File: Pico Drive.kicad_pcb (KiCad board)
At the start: 2 copper layers, 79.2 x 56.2 mm, 27 parts, among them J1 Conn_01x06_Male, J2 Conn_01x05, J3 Conn_01x03_Male, J4 Conn_01x06, J6 I2C, SW1 Reset, U1 Pico, U2 74AXP1T45GWH, U3 74AHCT1G125DBVTG4

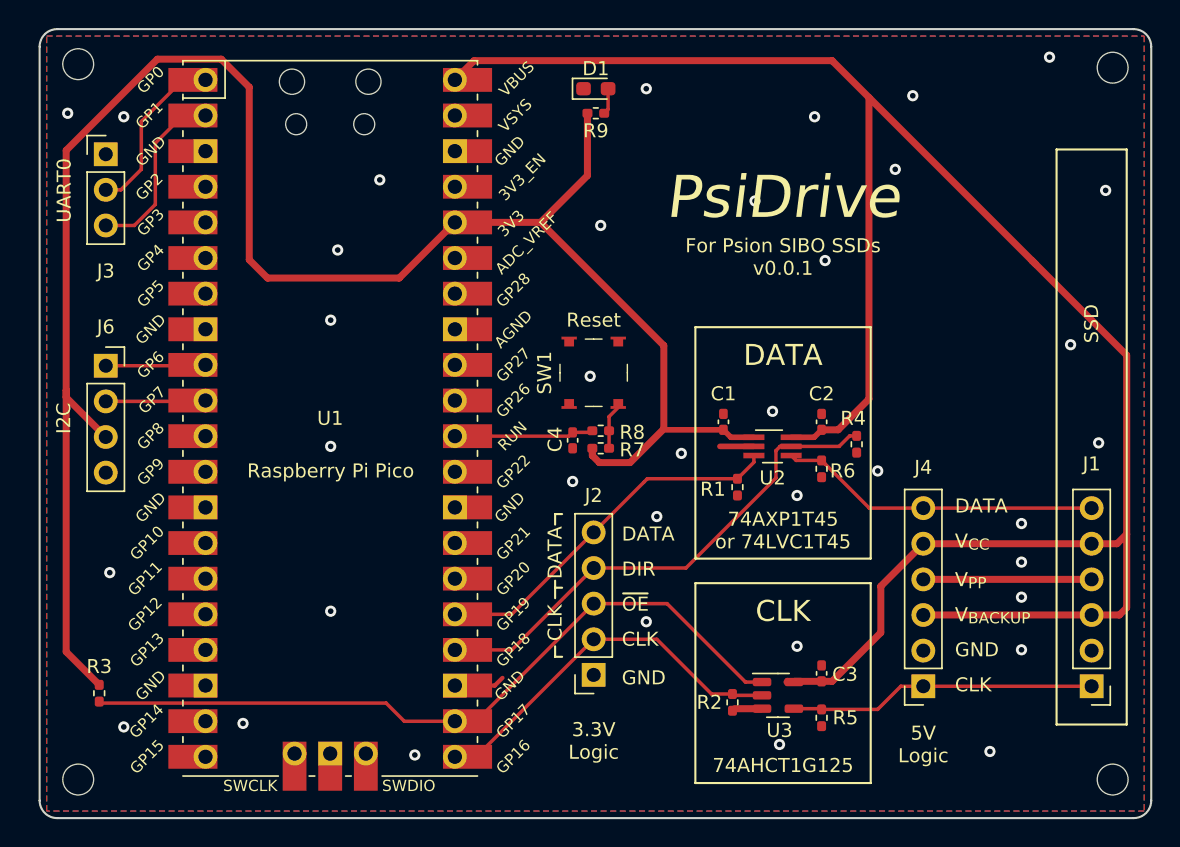
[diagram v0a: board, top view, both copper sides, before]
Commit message: Changed all 0402 components to 0805
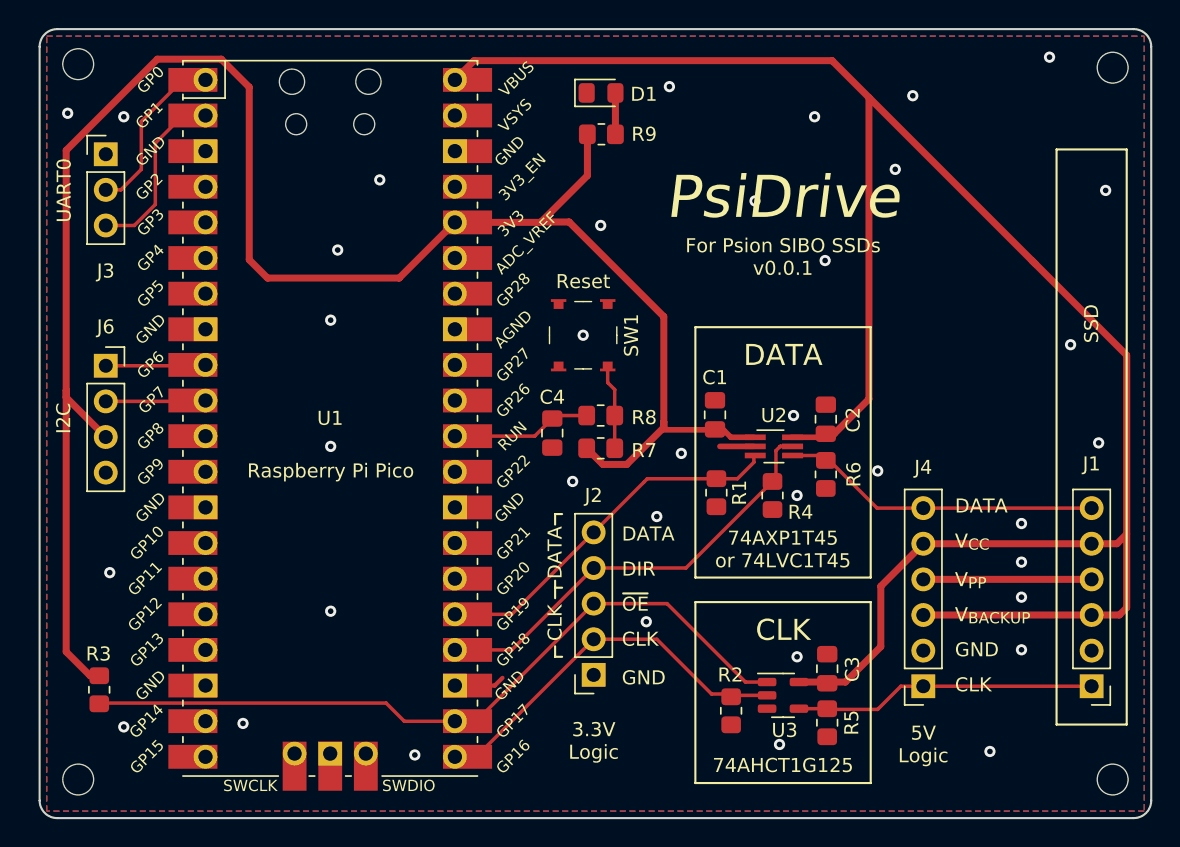
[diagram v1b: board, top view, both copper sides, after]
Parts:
- C1, C2, C3, C4: footprint Capacitor_SMD:C_0402_1005Metric_Pad0.74x0.62mm_HandSolder -> Capacitor_SMD:C_0805_2012Metric_Pad1.18x1.45mm_HandSolder
- D1: footprint LED_SMD:LED_0603_1608Metric_Pad1.05x0.95mm_HandSolder -> LED_SMD:LED_0805_2012Metric_Pad1.15x1.40mm_HandSolder
- R1, R2, R3, R4, R5, R6, R7, R8, R9: footprint Resistor_SMD:R_0402_1005Metric_Pad0.72x0.64mm_HandSolder -> Resistor_SMD:R_0805_2012Metric_Pad1.20x1.40mm_HandSolder
- moved R4 7.02 mm to (68.0, 54.5)
- moved SW1 2.78 mm to (54.5, 43.1)
- moved R1 1.55 mm to (64.0, 54.3)
- moved R9 1.55 mm to (55.8, 28.8)
- moved C4 1.54 mm to (52.3, 50.0)
- moved R8 1.09 mm to (55.8, 48.8)
- moved C1 0.78 mm to (63.9, 48.8)
- moved R2 0.61 mm to (65.0, 69.8)
- moved R5 0.53 mm to (71.9, 70.7)
- moved C3 0.52 mm to (71.9, 66.8)
- moved R6 0.50 mm to (71.8, 53.0)
- moved D1 0.48 mm to (55.8, 25.8)
- moved U3 0.36 mm to (68.8, 68.8)
- moved C2 0.35 mm to (71.8, 49.1)
- moved R3 0.25 mm to (20.0, 68.3)
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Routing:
- net /DATA_DIR: track 36.9 -> 31.9 mm
- net Net-(R7-Pad2): track 3.18 -> 5.79 mm
- net GND: track 8.21 -> 6.04 mm
- net Net-(D1-A): track 1.86 -> 2.95 mm

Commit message: Swapped LED and reset switch, made more space
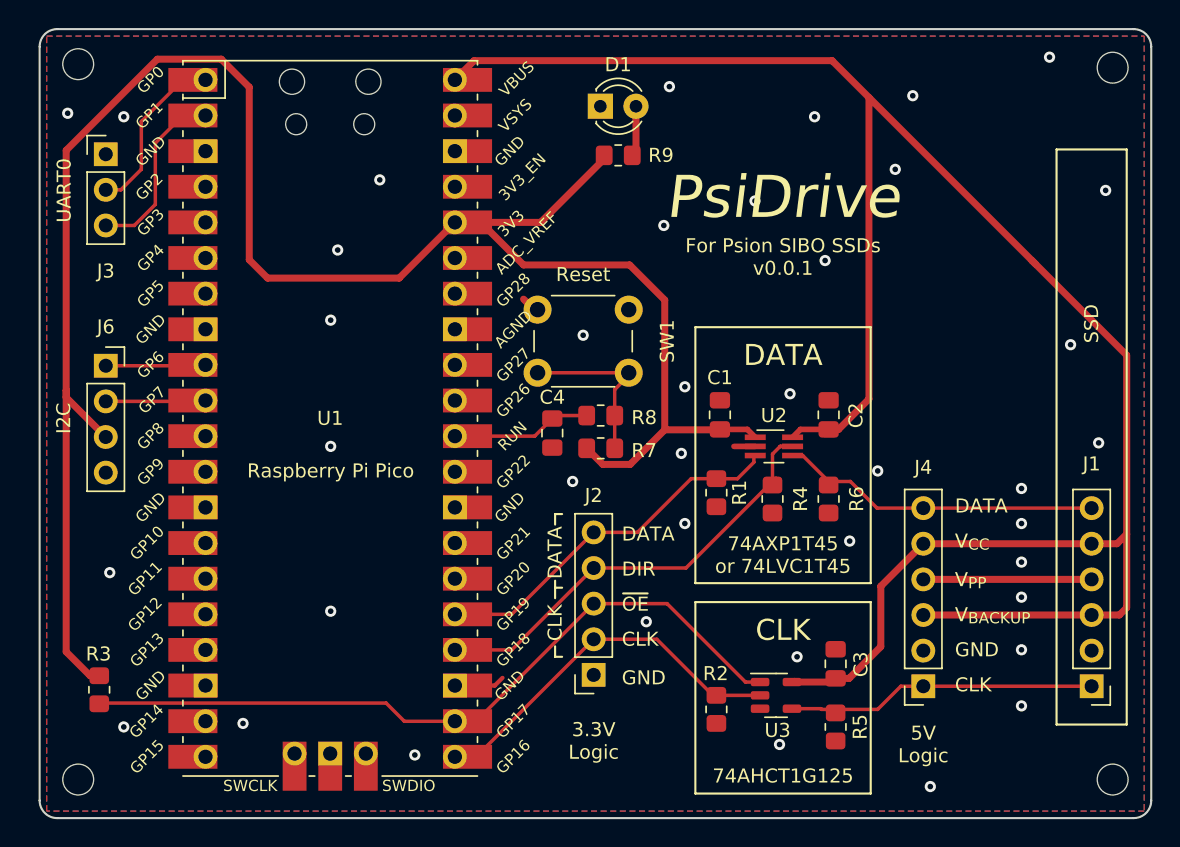
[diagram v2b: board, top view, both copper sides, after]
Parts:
- D1: footprint LED_SMD:LED_0805_2012Metric_Pad1.15x1.40mm_HandSolder -> LED_THT:LED_D3.0mm_Clear
- SW1: footprint digikey-footprints:Switch_Tactile_SMD_4.5x4.5mm_TL3315NF160Q -> Button_Switch_THT:SW_PUSH_6mm_H5mm
- moved SW1 3.73 mm to (51.2, 41.2), turned to 0 degrees
- moved R9 1.92 mm to (57.0, 30.2)
- moved R6 1.76 mm to (72.0, 54.8)
- moved R2 1.05 mm to (64.0, 69.8)
- moved D1 0.95 mm to (55.7, 26.8)
- moved C3 0.69 mm to (72.5, 66.5)
- moved R5 0.67 mm to (72.5, 71.0)
- moved U3 0.50 mm to (68.2, 68.8)
- moved C2 0.37 mm to (72.0, 48.8)
- moved C1 0.35 mm to (64.2, 48.8)
- moved R4 0.25 mm to (68.0, 54.8)
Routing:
- net Net-(R7-Pad2): track 5.79 -> 12.8 mm
- net +3V3: track 136.5 -> 142.7 mm
- net +5V: track 148.2 -> 149.9 mm
- net Net-(D1-A): track 2.95 -> 3.61 mm
- net GND: track 6.04 -> 6.20 mm, vias 37 -> 40

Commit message: Added pullups and decoupling for I2C
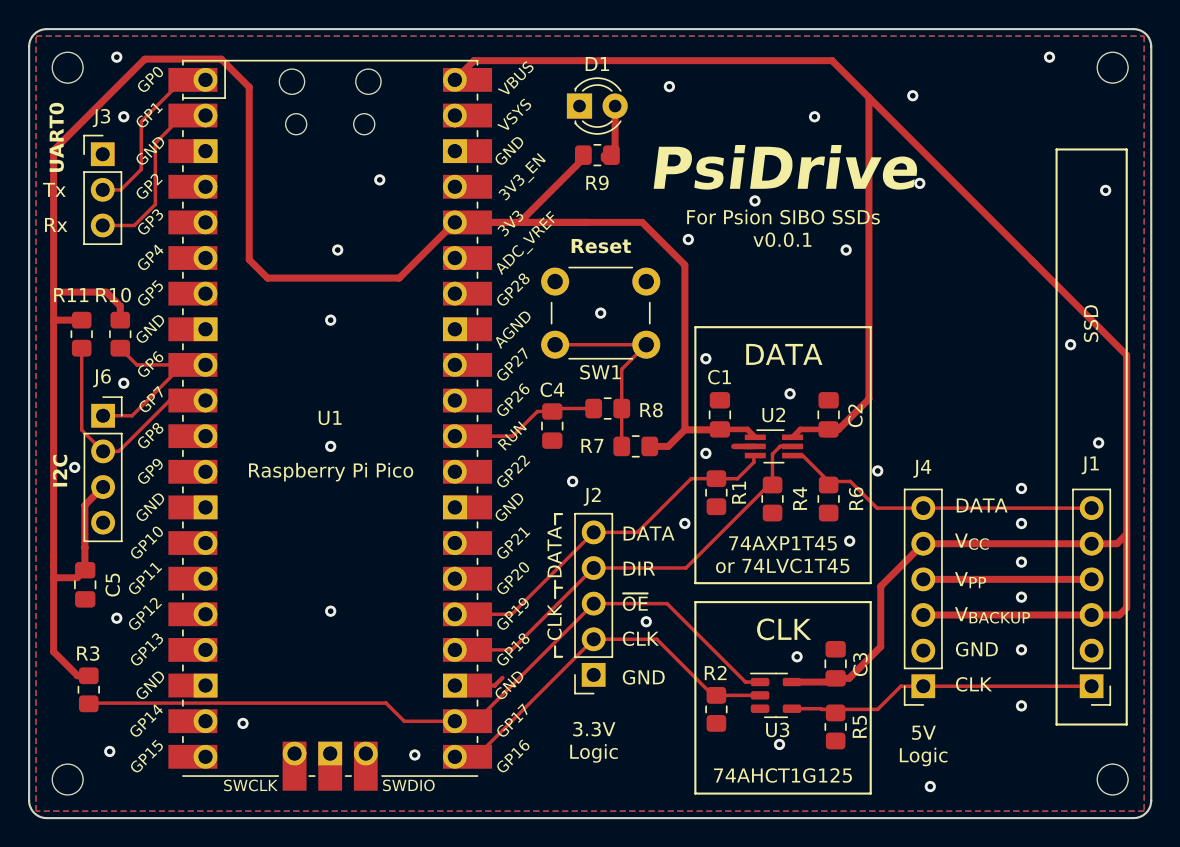
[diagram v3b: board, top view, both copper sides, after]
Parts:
- added C5: 100n, Capacitor_SMD:C_0805_2012Metric_Pad1.18x1.45mm_HandSolder, F.Cu at (19.0, 60.9)
- added R10: 10k, Resistor_SMD:R_0805_2012Metric_Pad1.20x1.40mm_HandSolder, F.Cu at (21.5, 43.0)
- added R11: 10k, Resistor_SMD:R_0805_2012Metric_Pad1.20x1.40mm_HandSolder, F.Cu at (18.8, 43.0)
- moved J6 3.57 mm to (20.3, 48.8)
- moved R7 2.50 mm to (58.2, 51.0), turned to 180 degrees
- moved SW1 2.36 mm to (52.5, 39.2)
- moved D1 1.49 mm to (54.2, 26.7)
- moved R9 1.49 mm to (55.5, 30.2)
- moved H1 0.79 mm to (17.8, 24.0)
- moved H2 0.75 mm to (17.8, 74.8)
- moved R3 0.75 mm to (19.3, 68.3)
- moved R8 0.71 mm to (56.2, 48.3)
- moved C4 0.50 mm to (52.3, 49.5)
- moved J3 0.22 mm to (20.2, 30.2)
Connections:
- U1 pad 11: /UART1_TX -> unconnected-(U1-GPIO8-Pad11)
- U1 pad 12: /UART1_RX -> unconnected-(U1-GPIO9-Pad12)
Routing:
- net +3V3: track 142.7 -> 155.8 mm
- net /I2C1_SCL: track 7.13 -> 16.9 mm
- net /I2C1_SDA: track 7.13 -> 15.5 mm
- net Net-(R7-Pad2): track 12.8 -> 13.9 mm
- net GND: track 6.20 -> 5.14 mm, vias 40 -> 42
- net /~{CLK_OE}: track 53.3 -> 54.1 mm
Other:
- board size 79.2 x 56.2 mm -> 80 x 56.2 mm
- board text added: "Rx"
- board text added: "Tx"
